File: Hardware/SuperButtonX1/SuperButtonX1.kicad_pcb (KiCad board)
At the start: 2 copper layers, 53.2 x 53.2 mm, 25 parts, among them J101 USBC, J103 EXT_LED, SW101 Switch, SW102 PROG, U101 CH552G

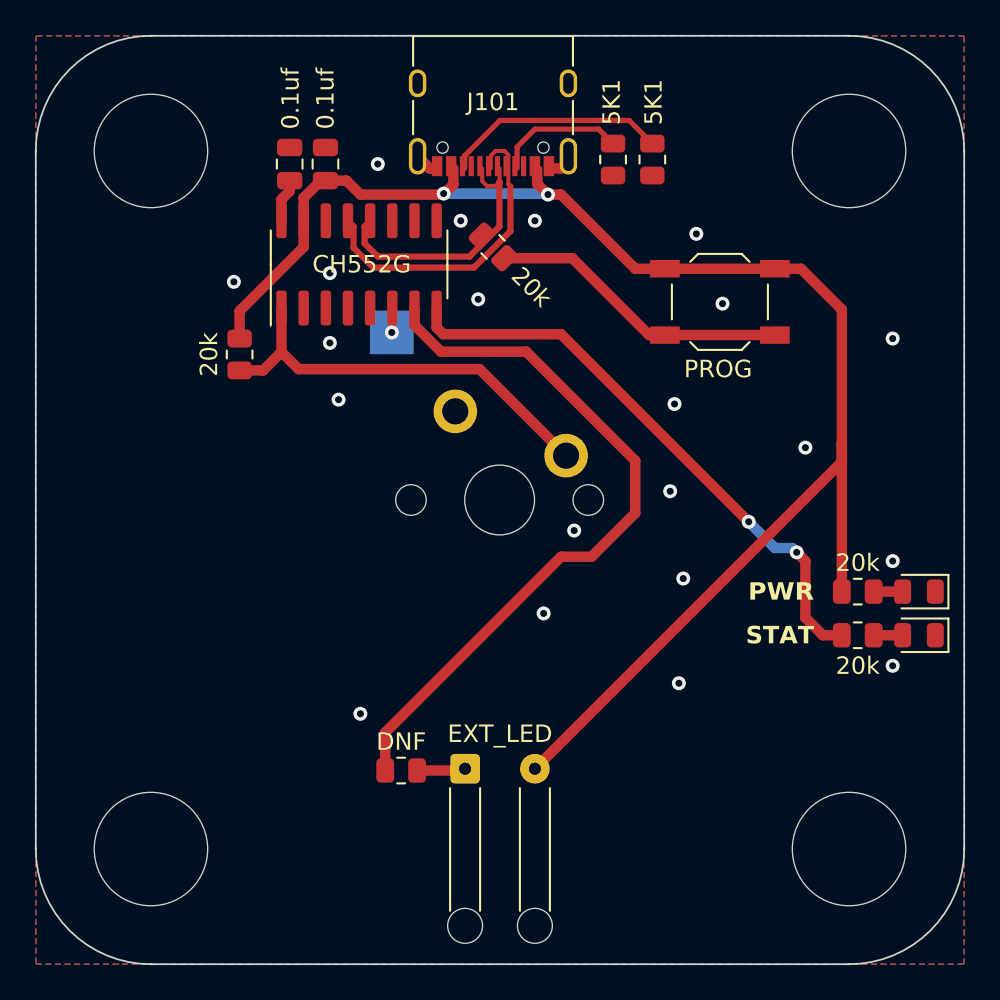
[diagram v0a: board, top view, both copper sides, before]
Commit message: Feat/Variants (#4)
Co-authored-by: Jack Jewett <jewett818@gmail.com>
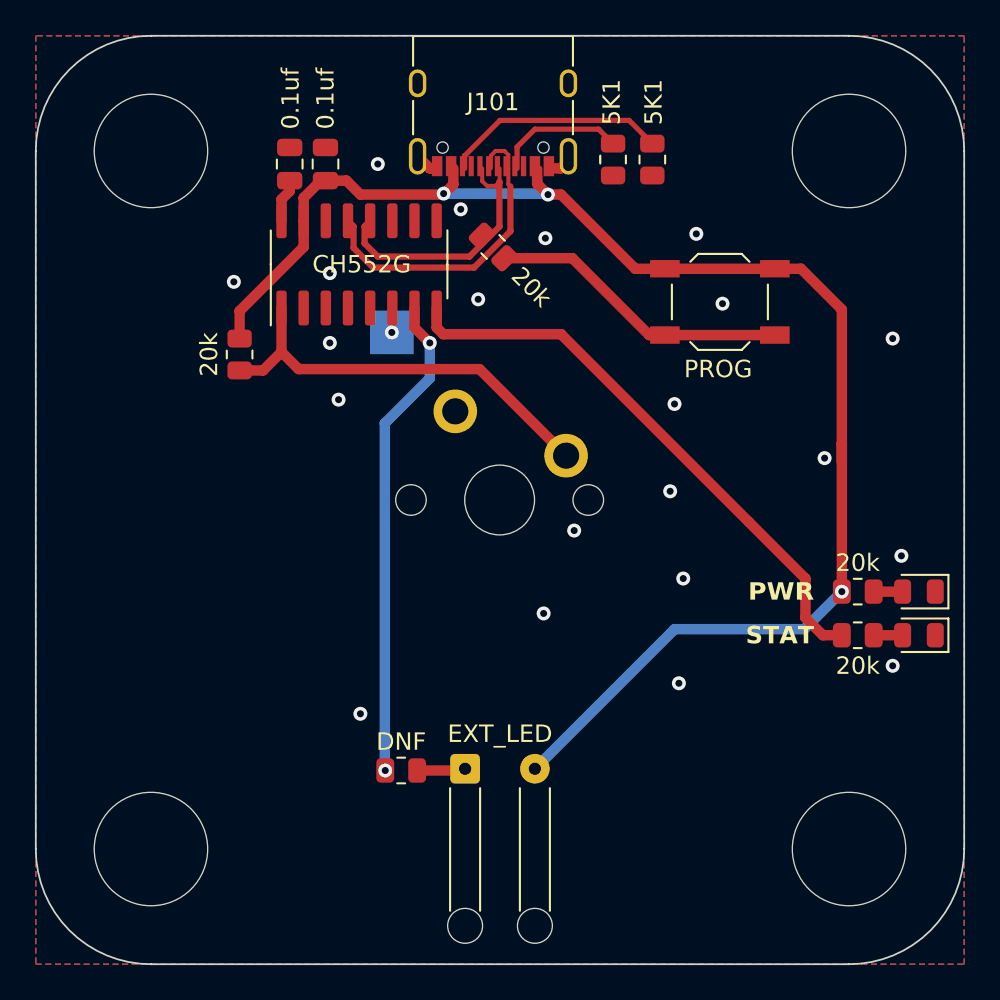
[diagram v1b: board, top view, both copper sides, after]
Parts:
- moved G*** 5.37 mm to (190.4, 89.6)
- moved REF** 3.60 mm to (153.8, 96.4)
- moved REF** 3.60 mm to (153.5, 86.8)
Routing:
- net /EXT: track 41.6 -> 27.9 mm, vias 0 -> 2
- net +5V: track 90.7 -> 87.6 mm, vias 2 -> 3
- net /STAT: track 33.5 -> 33.0 mm, vias 2 -> 0
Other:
- board text added: "By FRC 1721 Tidal Force Concord, NH https://www.frc1721.org/ ${FULL_REVISION}"
- board text added: "Programmable Single Key Keyboard"
- board text removed: "Super Buttton By FRC 1721 Tidal Force https://www.frc1721.org/ ${FULL_REVISION}"

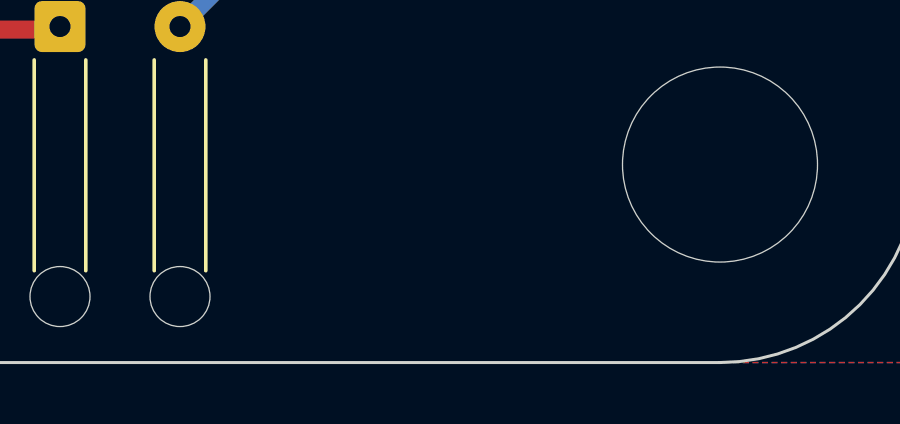
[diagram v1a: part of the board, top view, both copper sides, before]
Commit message: Add JLCJLCJLC to boards
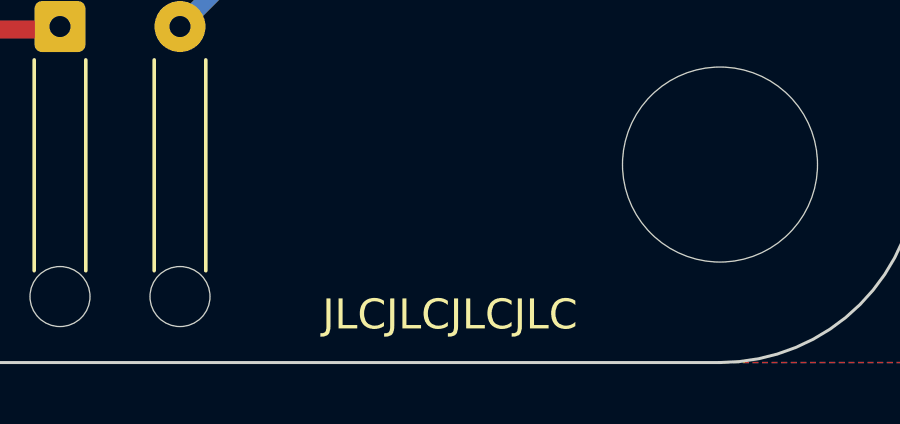
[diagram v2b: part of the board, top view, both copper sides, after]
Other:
- board text added: "JLCJLCJLCJLC"
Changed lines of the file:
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@@
     (effects (font (size 1 1) (thickness 0.25) bold) (justify left top mirror))
+  )
+  (gr_text "JLCJLCJLCJLC" (at 183 115) (layer "F.SilkS")
+    (effects (font (size 1 1) (thickness 0.25)))
   )
   (dimension (type aligned) (layer "Dwgs.User")
